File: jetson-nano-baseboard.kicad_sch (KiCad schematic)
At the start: 3 parts

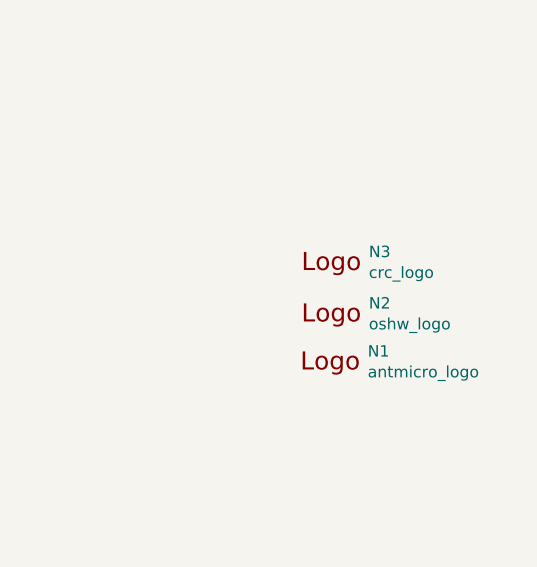
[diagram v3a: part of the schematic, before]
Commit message: Standardize components
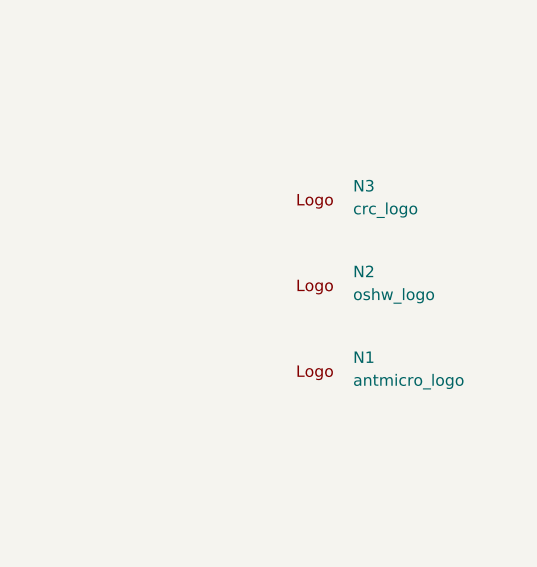
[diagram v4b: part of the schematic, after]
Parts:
- N1: footprint jetson-nano-baseboard-footprints:antmicro-logo_scaled_15mm -> antmicro-footprints:antmicro-logo_scaled_15mm; symbol jetson-nano-baseboard:antmicro_logo -> antmicroMechanicalParts:antmicro_logo; Author (none) -> Antmicro; License (none) -> Apache-2.0; Manufacturer (none) -> None
- N2: footprint jetson-nano-baseboard-footprints:oshw-logo -> antmicro-footprints:oshw-logo; symbol jetson-nano-baseboard:oshw_logo -> antmicroMechanicalParts:oshw_logo; Author (none) -> Antmicro; License (none) -> Apache-2.0; Manufacturer (none) -> None
- N3: footprint jetson-nano-baseboard-footprints:CRC_logo_15mm -> antmicro-footprints:CRC_logo_15mm; symbol jetson-nano-baseboard:crc_logo -> antmicroMechanicalParts:crc_logo; Author (none) -> Antmicro; License (none) -> Apache-2.0; Manufacturer (none) -> None
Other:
- moved on the sheet: N1, N2, N3

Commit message: [#56834] Fix components links
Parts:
- N1: footprint antmicro-footprints:antmicro-logo_scaled_15mm -> jetson-nano-baseboard-footprints:antmicro-logo; symbol antmicroMechanicalParts:antmicro_logo -> jetson-nano-baseboard:antmicro_logo; Manufacturer None -> (none)
- N2: footprint antmicro-footprints:oshw-logo -> jetson-nano-baseboard-footprints:oshw-logo; symbol antmicroMechanicalParts:oshw_logo -> jetson-nano-baseboard:oshw_logo; Manufacturer None -> (none)
- N3: footprint antmicro-footprints:CRC_logo_15mm -> jetson-nano-baseboard-footprints:CRC_logo_15mm; symbol antmicroMechanicalParts:crc_logo -> jetson-nano-baseboard:crc_logo; Manufacturer None -> (none)

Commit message: [#57913] fix 2309413-1
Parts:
- N1: footprint jetson-nano-baseboard-footprints:antmicro-logo -> antmicro-footprints:antmicro-logo; symbol jetson-nano-baseboard:antmicro_logo -> antmicroMechanicalParts:antmicro_logo
- N2: footprint jetson-nano-baseboard-footprints:oshw-logo -> antmicro-footprints:oshw-logo; symbol jetson-nano-baseboard:oshw_logo -> antmicroMechanicalParts:oshw_logo
- N3: footprint jetson-nano-baseboard-footprints:CRC_logo_15mm -> antmicro-footprints:CRC_logo_15mm; symbol jetson-nano-baseboard:crc_logo -> antmicroMechanicalParts:crc_logo
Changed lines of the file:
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@@
     (effects (font (size 1.524 1.524)) (justify left bottom))
   )
-  (symbol (lib_id "jetson-nano-baseboard:antmicro_logo") (at 381 247.65 0) (unit 1)
+  (symbol (lib_id "antmicroMechanicalParts:antmicro_logo") (at 381 247.65 0) (unit 1)
     (in_bom yes) (on_board yes) (dnp no) (fields_autoplaced)
     (property "Reference" "N1" (at 387.35 245.3575 0)
@@
       (effects (font (size 1.27 1.27)) (justify left))
     )
-    (property "Footprint" "jetson-nano-baseboard-footprints:antmicro-logo" (at 378.46 241.3 0)
+    (property "Footprint" "antmicro-footprints:antmicro-logo" (at 378.46 241.3 0)
       (effects (font (size 1.27 1.27)) (justify left) hide)
     )
@@
     )
   )
-  (symbol (lib_id "jetson-nano-baseboard:oshw_logo") (at 381 238.125 0) (unit 1)
+  (symbol (lib_id "antmicroMechanicalParts:oshw_logo") (at 381 238.125 0) (unit 1)
     (in_bom yes) (on_board yes) (dnp no) (fields_autoplaced)
     (property "Reference" "N2" (at 387.35 235.8325 0)
@@
       (effects (font (size 1.27 1.27)) (justify left))
     )
-    (property "Footprint" "jetson-nano-baseboard-footprints:oshw-logo" (at 381.508 244.221 0)
+    (property "Footprint" "antmicro-footprints:oshw-logo" (at 381.508 244.221 0)
       (effects (font (size 1.27 1.27)) (justify left) hide)
     )
@@
     )
   )
-  (symbol (lib_id "jetson-nano-baseboard:crc_logo") (at 381 228.6 0) (unit 1)
+  (symbol (lib_id "antmicroMechanicalParts:crc_logo") (at 381 228.6 0) (unit 1)
     (in_bom yes) (on_board yes) (dnp no) (fields_autoplaced)
     (property "Reference" "N3" (at 387.35 226.3075 0)
@@
       (effects (font (size 1.27 1.27)) (justify left))
     )
-    (property "Footprint" "jetson-nano-baseboard-footprints:CRC_logo_15mm" (at 381.508 234.696 0)
+    (property "Footprint" "antmicro-footprints:CRC_logo_15mm" (at 381.508 234.696 0)
       (effects (font (size 1.27 1.27)) (justify left) hide)
     )
